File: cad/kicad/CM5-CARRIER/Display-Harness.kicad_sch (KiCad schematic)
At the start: 13 parts, among them J801 HDMI_TO_LID_DISPLAY, J802 TOUCH_USB_HOST, J803 LID_DISPLAY_12V, U801 TPD4E05U06DQA, U802 TPD4E05U06DQA, U803 TPD4E05U06DQA, U804 TPD4E05U06DQA

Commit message: Define serviceable lid display cable bundle
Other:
- note added: "Acceptance: full lid travel plus 300 mm panel lift / 45 degree tilt; no connector tension or hinge-line bend."
- note added: "Carrier connectors face down. Store released loops clear of fans, PSU airflow, board keepouts and sharp edges."
- note added: "H03A HDMI, H03B USB touch, H03C 12 V: 1000 +/- 25 mm each, with separate retained hinge and service loops."
- note added: "No local display eFuse. Use the upstream AUX_12V branch fuse and H03C keyed 18 AWG harness."
- note removed: "All three carrier connectors are underside-facing and remain below the top panel; they do not add panel cutouts."
- note removed: "Bundle HDMI, USB A-to-B, and 12 V conductors through the centered hinge-edge notch with a common abrasion sleeve."
- note removed: "No local display eFuse. Use the upstream AUX_12V branch fuse and a keyed 18 AWG harness."
- note removed: "Provide a service loop for full lid travel, clamp the bundle on both sides, and keep bend radius outside the hinge pinch line."
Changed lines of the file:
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@@
 		)
 	)
-	(text "No local display eFuse. Use the upstream AUX_12V branch fuse and a keyed 18 AWG harness."
+	(text "No local display eFuse. Use the upstream AUX_12V branch fuse and H03C keyed 18 AWG harness."
 		(exclude_from_sim no)
 		(at 400 455 0.0000)
@@
 		)
 	)
-	(text "Bundle HDMI, USB A-to-B, and 12 V conductors through the centered hinge-edge notch with a common abrasion sleeve."
+	(text "H03A HDMI, H03B USB touch, H03C 12 V: 1000 +/- 25 mm each, with separate retained hinge and service loops."
 		(exclude_from_sim no)
 		(at 45 510 0.0000)
 		(effects
 			(font
-				(size 0.82 0.82)
+				(size 0.76 0.76)
 			)
 		)
 	)
-	(text "Provide a service loop for full lid travel, clamp the bundle on both sides, and keep bend radius outside the hinge pinch line."
+	(text "Acceptance: full lid travel plus 300 mm panel lift / 45 degree tilt; no connector tension or hinge-line bend."
 		(exclude_from_sim no)
 		(at 45 520 0.0000)
 		(effects
 			(font
-				(size 0.82 0.82)
+				(size 0.76 0.76)
 			)
 		)
 	)
-	(text "All three carrier connectors are underside-facing and remain below the top panel; they do not add panel cutouts."
+	(text "Carrier connectors face down. Store released loops clear of fans, PSU airflow, board keepouts and sharp edges."
 		(exclude_from_sim no)
 		(at 45 530 0.0000)
 		(effects
 			(font
-				(size 0.82 0.82)
+				(size 0.76 0.76)
 			)
 		)

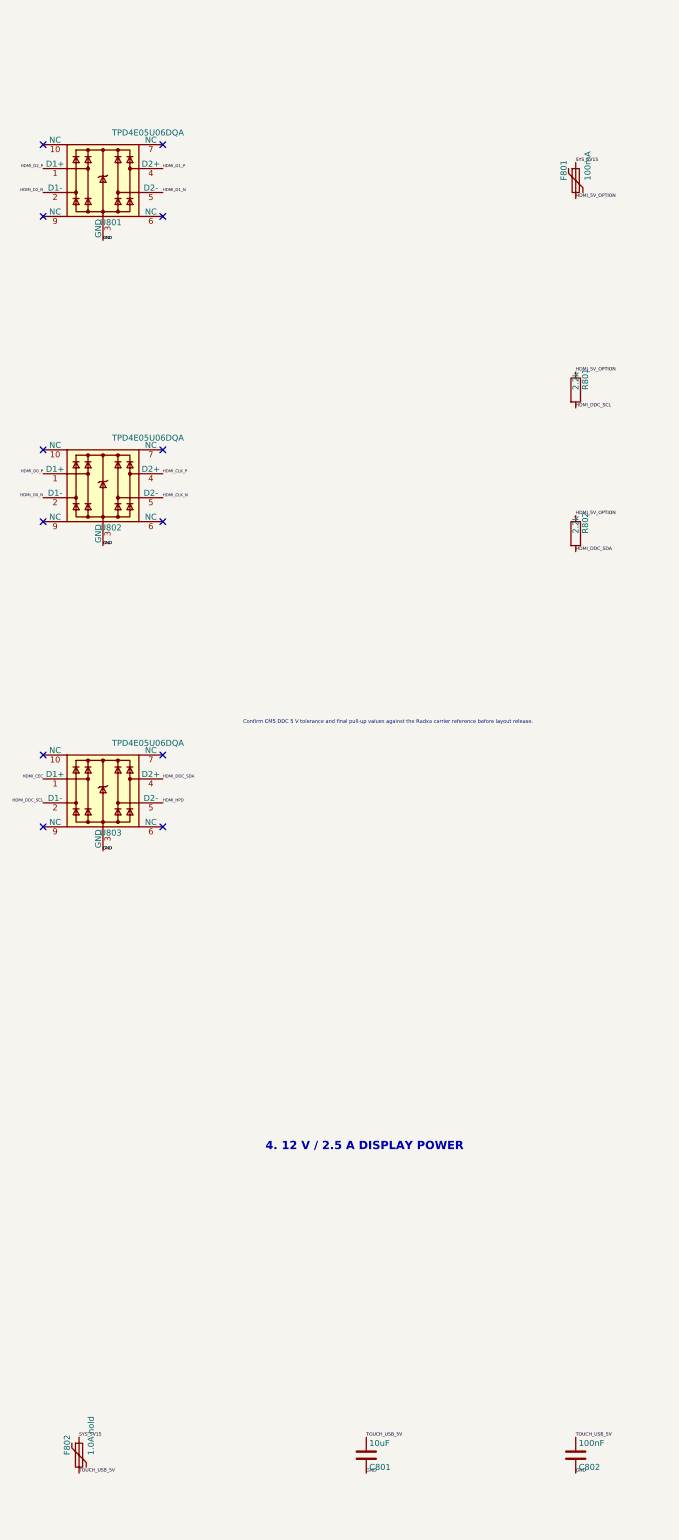
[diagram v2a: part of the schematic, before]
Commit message: Complete A1 detailed carrier and audio capture
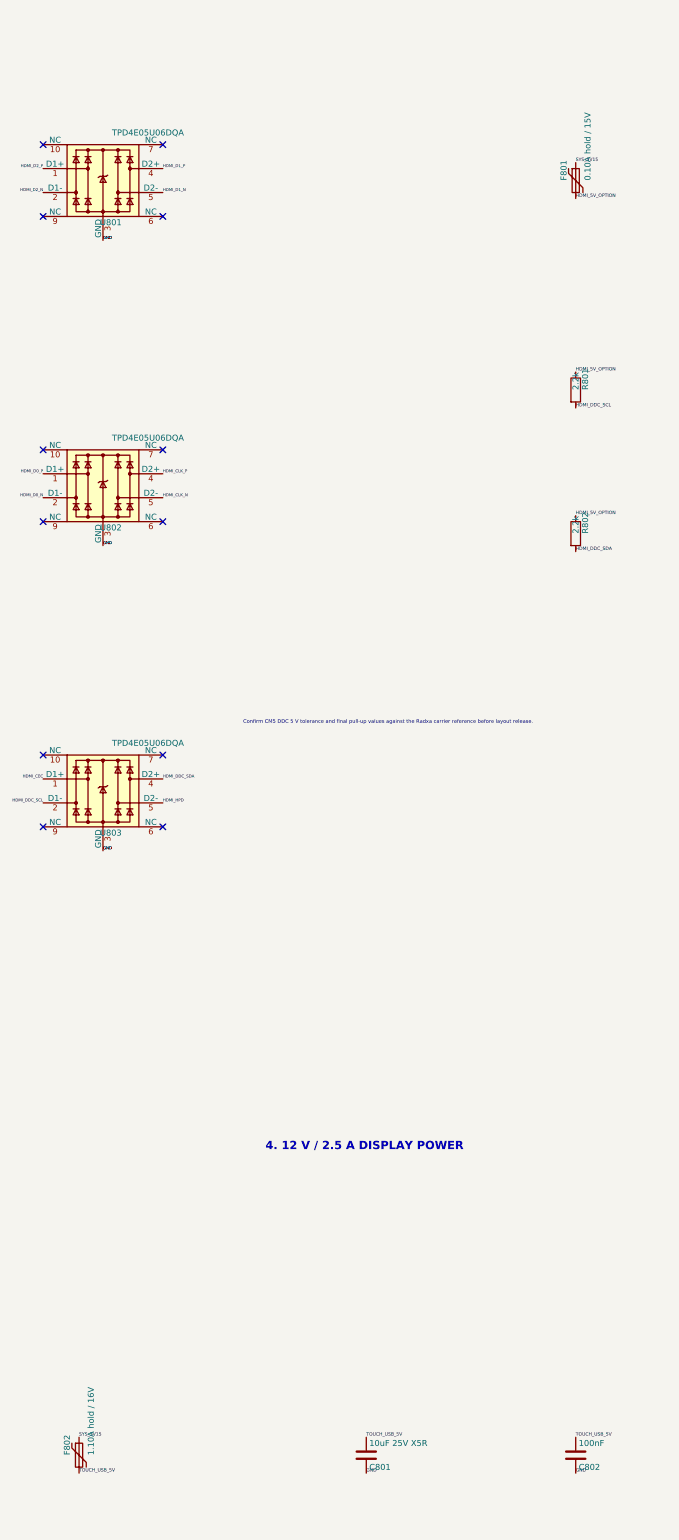
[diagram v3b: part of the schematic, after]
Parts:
- removed F802: 1.0A hold, symbol Device:Polyfuse
- added J803: LID_DISPLAY_12V, Connector_Molex:Molex_Micro-Fit_3.0_43045-0412_2x02_P3.00mm_Vertical, symbol Connector_Generic:Conn_02x02_Odd_Even
- C801: value 10uF -> 10uF 25V X5R; footprint (none) -> Capacitor_SMD:C_0603_1608Metric; MPN (none) -> GRM188R61E106MA73D; Manufacturer (none) -> Murata
- C802: footprint (none) -> Capacitor_SMD:C_0402_1005Metric; MPN (none) -> C1005X7R1H104K050BB; Manufacturer (none) -> TDK
- F801: value 100mA -> 0.10A hold / 15V; footprint (none) -> Fuse:Fuse_0603_1608Metric; MPN (none) -> 0603L010YR; Manufacturer (none) -> Littelfuse
- F802: renamed from J803; value LID_DISPLAY_12V -> 1.10A hold / 16V; footprint Connector_Molex:Molex_Micro-Fit_3.0_43045-0412_2x02_P3.00mm_Vertical -> Fuse:Fuse_1206_3216Metric; symbol Connector_Generic:Conn_02x02_Odd_Even -> Device:Polyfuse; MPN 43045-0412 -> 1206L110/16WR; Manufacturer Molex -> Littelfuse
- R801, R802: footprint (none) -> Resistor_SMD:R_0603_1608Metric; MPN (none) -> RC0603FR-072K2L; Manufacturer (none) -> Yageo
- U801, U802, U803, U804: footprint (none) -> Package_SON:USON-10_2.5x1.0mm_P0.5mm
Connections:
- net DISPLAY_12V: now also J803.1 (Pin_1), J803.2 (Pin_2); no longer F802.1 (Pin_1), F802.2 (Pin_2)
- net GND: now also J803.3 (Pin_3), J803.4 (Pin_4); no longer F802.3 (Pin_3), F802.4 (Pin_4)
- net SYS_5V15: now also F802.1
- net TOUCH_USB_5V: now also F802.2

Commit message: Lock CM5 power and radio interfaces before routing
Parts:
- added C805: 470nF, Capacitor_SMD:C_0603_1608Metric, symbol Device:C
- added C806, C807: 10uF 25V X7R, Capacitor_SMD:C_0805_2012Metric, symbol Device:C
- added C808, C809, C810: 22uF 10V X7R, Capacitor_SMD:C_0805_2012Metric, symbol Device:C
- added L805: 2.2uH / 3.7A, Inductor_SMD:L_Coilcraft_XxL4040, symbol Device:L
- added R805: 26.1k 0.1%, Resistor_SMD:R_0603_1608Metric, symbol Device:R
- added R806: 4.99k 0.1%, Resistor_SMD:R_0603_1608Metric, symbol Device:R
- added R807: 7.5k S-CONF, Resistor_SMD:R_0603_1608Metric, symbol Device:R
- added U805: TPS62913RPU, Package_DFN_QFN:Texas_RPU0010A_VQFN-HR-10_2x2mm_P0.5mm, symbol CM5Carrier:TPS62913RPU
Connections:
- net GND: now also C805.2, C806.2, C807.2, C808.2, C809.2, C810.2, R806.2, R807.2, U805.4 (PGND), U805.7 (PSNS)
- net HDMI_5V_OPTION renamed HDMI_5V_OUT
- net SYS_5V15 renamed IO_5V0
- net IO_5V0: now also C808.1, C809.1, C810.1, L805.2, R805.1, U805.3 (VO)
- new net DISPLAY_IO_12V: C806.1, C807.1, U805.1 (EN/SYNC), U805.6 (VIN)
- new net IO5V0_FB: R805.2, R806.1, U805.9 (FB)
- new net IO5V0_NRSS: C805.1, U805.8 (NR/SS)
- new net IO5V0_SCONF: R807.1, U805.10 (S-CONF)
- new net IO5V0_SW: L805.1, U805.2 (SW)
- new net IO_5V0_PG: U805.5 (PG)
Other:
- note added: "3. DEDICATED IO_5V0 / 2 A BUCK"
- note added: "4. USB TOUCH HOST PORT"
- note added: "5. 12 V / 2.5 A DISPLAY POWER"
- note added: "6. HINGE-EDGE HARNESS BUILD"
- note added: "IO_5V0 feeds CM5 U13-B pin 106, HDMI source 5 V and USB-touch VBUS; no monitor-power eFuse."
- note removed: "3. USB TOUCH HOST PORT"
- note removed: "4. 12 V / 2.5 A DISPLAY POWER"
- note removed: "5. HINGE-EDGE HARNESS BUILD"

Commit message: Audit schematic logic against controlled datasheets
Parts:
- removed R801, R802: 2.2k, Resistor_SMD:R_0603_1608Metric, symbol Device:R
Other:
- note added: "HDMI DDC connects directly to the CM5 5 V DDC pins, matching Radxa CM5 IO V2.2; do not add duplicate carrier pull-ups."
- note removed: "Confirm CM5 DDC 5 V tolerance and final pull-up values against the Radxa carrier reference before layout release."
